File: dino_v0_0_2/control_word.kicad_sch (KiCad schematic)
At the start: 12 parts, among them U28 74LS138, U29 74LS138, U30 74LS138, U62 74LS02, U70 74LS138, U71 74LS138

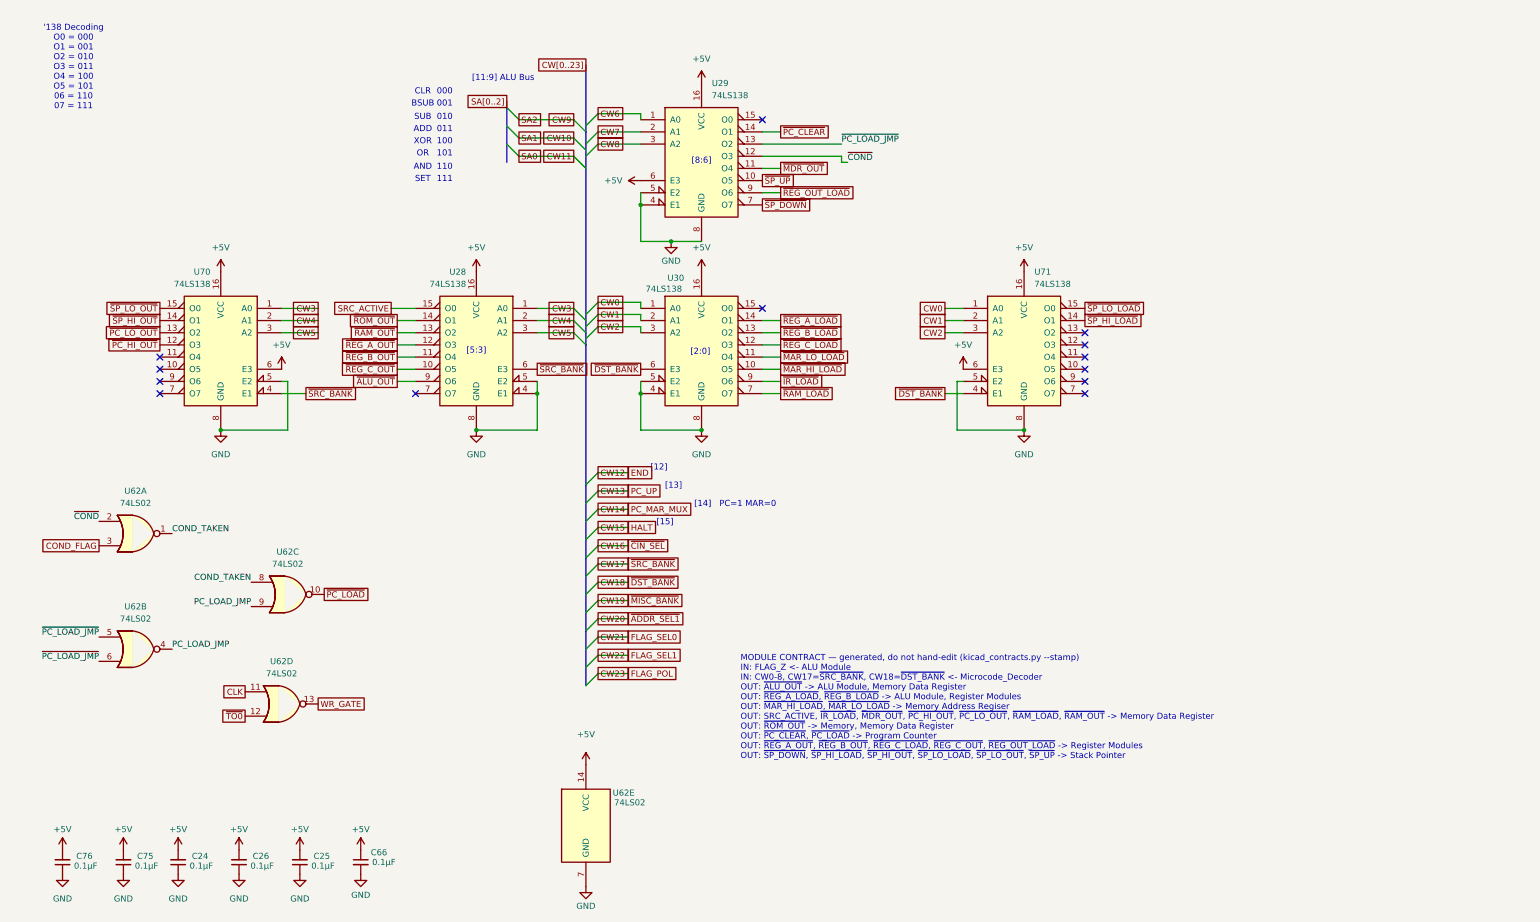
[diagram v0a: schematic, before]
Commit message: feat(int): draw the interrupt block; sheet cleanup pass
New sheet dino_v0_0_2/interrupt.kicad_sch (page 15): U80-U87, R28 4.7k
pull-up on ~{IRQ}, R29 100R on the block's CLK branch, C83-C90. Every
pin per PHASE_INT SECTION 3, checked against the plan with kicad_netlist
and kicad-cli (146 pins, 0 mismatches).

Old sheets (SECTION 3.2): U28.4 lifted off GND to INJECT; U61.3 to
END_OR_ACCEPT; U36.1 to PC_UP_GATED; U49 D0-3 cut from U48 Za-Zd and
routed through U87 as FLAG_NEXT0-3 / FLAG_D0-3; FLAG_C/Z/V/N and the
five decoder outputs made global. dino_serial: U104 74LS05, INTR ->
~{IRQ}, C4.

Placement pass on every sheet: bus entries and global labels no longer
share wires; M, CW, T, IRB and SA buses kept as labelled keys. Nets
diffed against HEAD per sheet: only the intended changes and a rotated
C29. Project ERC: 0 errors. MODULE CONTRACT stamps regenerated.

Co-Authored-By: Claude Fable 5.1 <noreply@anthropic.com>
Claude-Session: https://claude.ai/code/session_01JGxSS4MVUcaZdKZGtKroSg
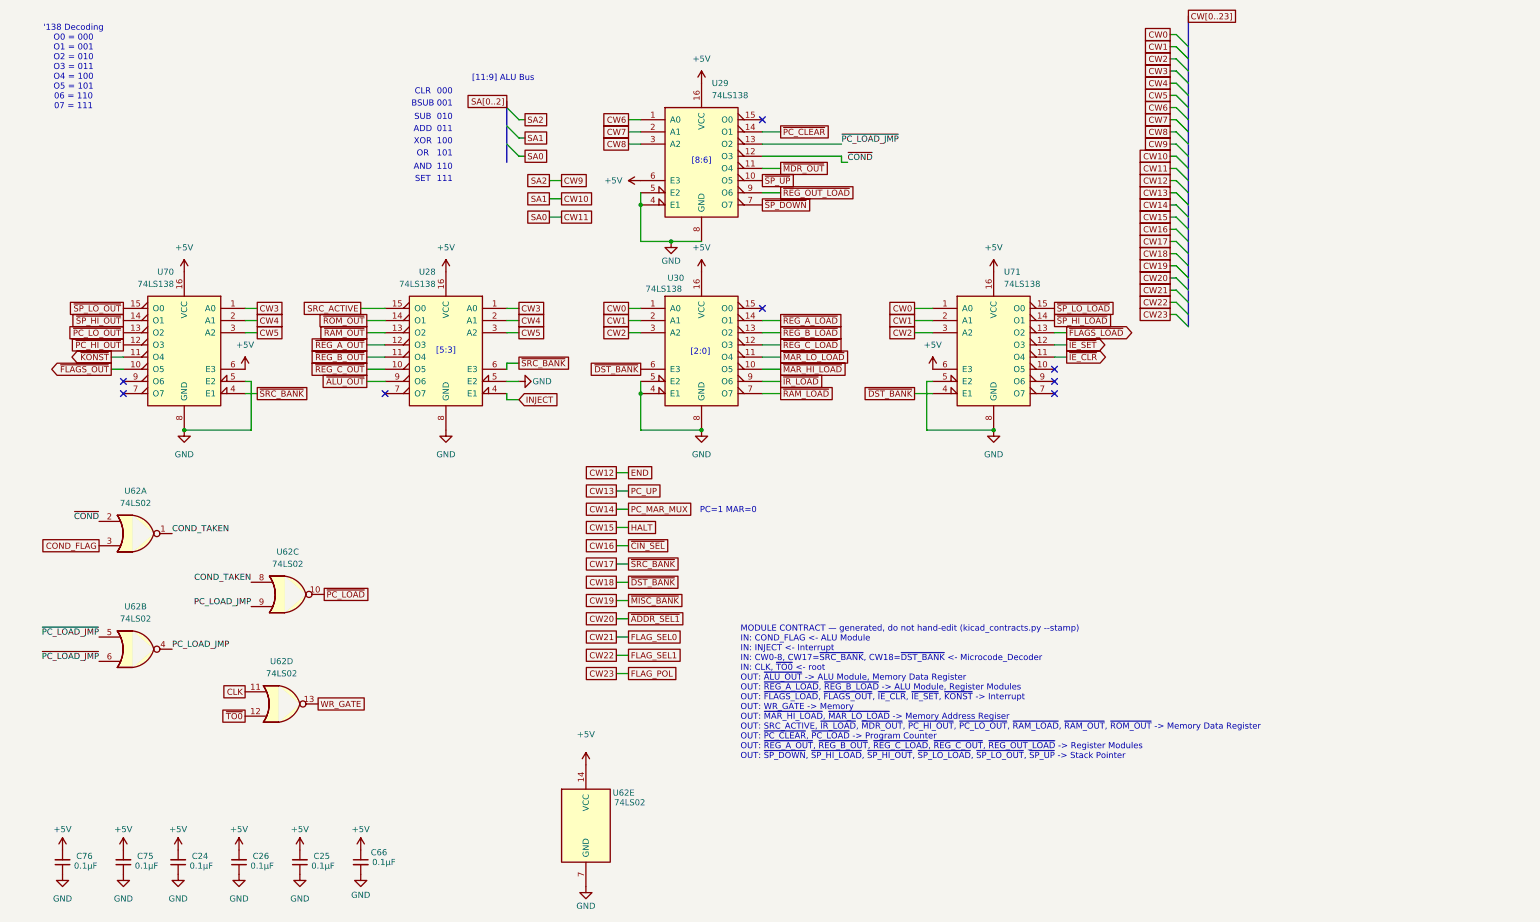
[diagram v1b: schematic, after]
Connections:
- net GND: no longer U28.4 (E1)
- net ~{FLAGS_OUT}: now reaches U70.10 (O5)
- net ~{KONST}: now reaches U70.11 (O4)
- net ~{IE_CLR}: now reaches U71.11 (O4)
- net ~{IE_SET}: now reaches U71.12 (O3)
- net ~{FLAGS_LOAD}: now reaches U71.13 (O2)
- new net INJECT: U28.4 (E1)
- no-connect marks 13 -> 8
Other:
- note added: "MODULE CONTRACT — generated, do not hand-edit (kicad_contracts.py --stamp) IN: COND_FLAG <- ALU Module IN: INJECT <- Interrupt IN: CW0-8, CW17=~{SRC_BANK}, CW18=~{DST_BANK} <- Microcode_Decoder IN: CLK, ~{TO0} <- root OUT: ~{ALU_OUT} -> ALU Module, Memory Data Register OUT: ~{REG_A_LOAD}, ~{REG_B_LOAD} -> ALU Module, Register Modules OUT: ~{FLAGS_LOAD}, ~{FLAGS_OUT}, ~{IE_CLR}, ~{IE_SET}, ~{KONST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"
- note removed: "MODULE CONTRACT — generated, do not hand-edit (kicad_contracts.py --stamp) IN: FLAG_Z <- ALU Module IN: CW0-8, CW17=~{SRC_BANK}, CW18=~{DST_BANK} <- Microcode_Decoder OUT: ~{ALU_OUT} -> ALU Module, Memory Data Register OUT: ~{REG_A_LOAD}, ~{REG_B_LOAD} -> ALU Module, Register Modules OUT: ~{MAR_HI_LOAD}, ~{MAR_LO_LOAD} -> Memory Address Regiser OUT: SRC_ACTIVE, ~{IR_LOAD}, ~{MDR_OUT}, ~{PC_HI_OUT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"
- note removed: "[12]"
- note removed: "[13]"
- note removed: "[14]"
- note removed: "[15]"
- moved on the sheet: U28, U70, U71
